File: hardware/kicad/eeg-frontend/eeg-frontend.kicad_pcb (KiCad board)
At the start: 2 copper layers, 60 x 60 mm, 77 parts, among them CN3 1000pF, CN4 1000pF, CN5 1000pF, CN6 1000pF, CN7 1000pF, J1 EEG Connector, J2 Conn_02x06_Top_Bottom, J3 Conn_01x08, J4 Conn_01x02, J5 Conn_01x02, Q1 DMP3099L, U1 ADS1299, U10 TPD4E1B06DCKR, U11 TPD4E1B06DCKR, U2 TPD4E1B06DCKR, U3 LM2664M6/NOPB, U4 MCP1754T-3302E/OT, U5 TPS72325DBV, U6 TLV70025_SOT23-5, U7 TPD4E1B06DCKR, U8 TPD4E1B06DCKR, U9 TPD4E1B06DCKR

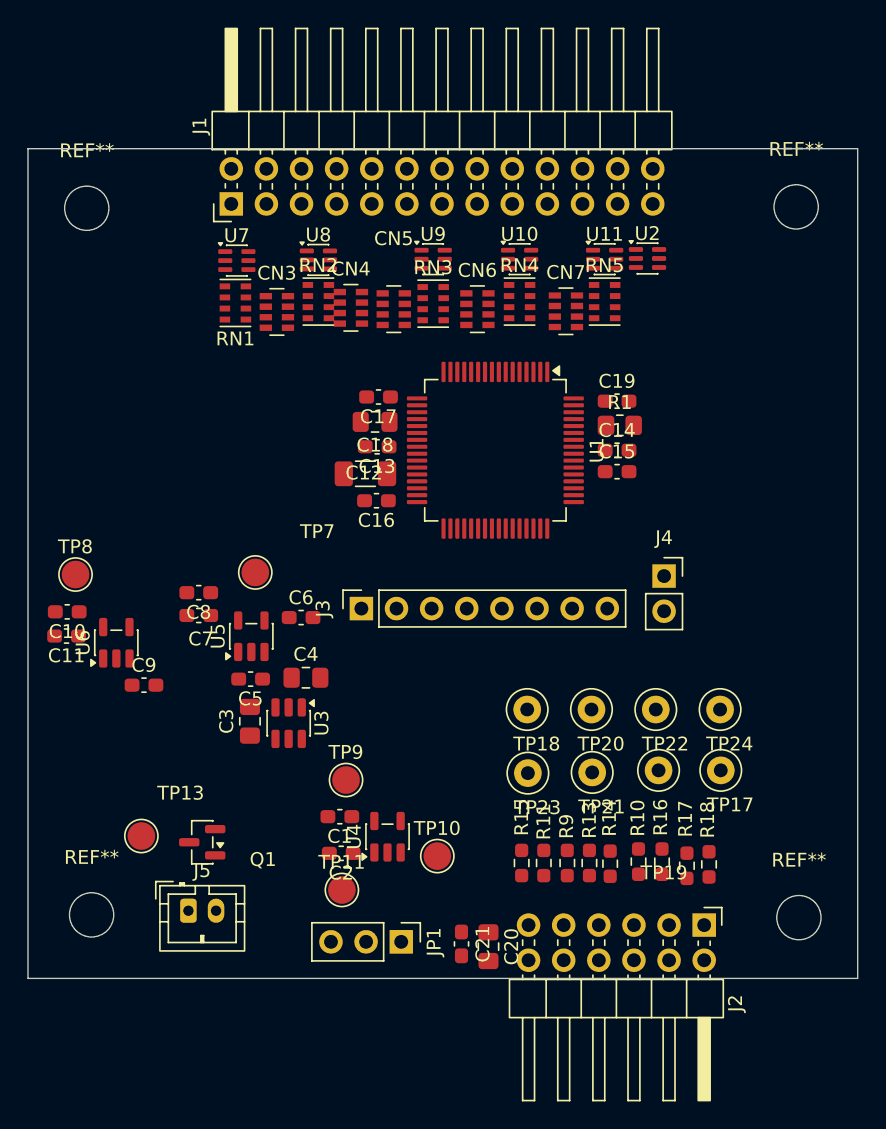
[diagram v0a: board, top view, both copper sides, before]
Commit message: 一旦できたと思ったPCB。 しかしPMODのコネクタの位置が左右で逆で、このまま刺すとGNDの一に通常のデータ信号的なのが来てしまう。
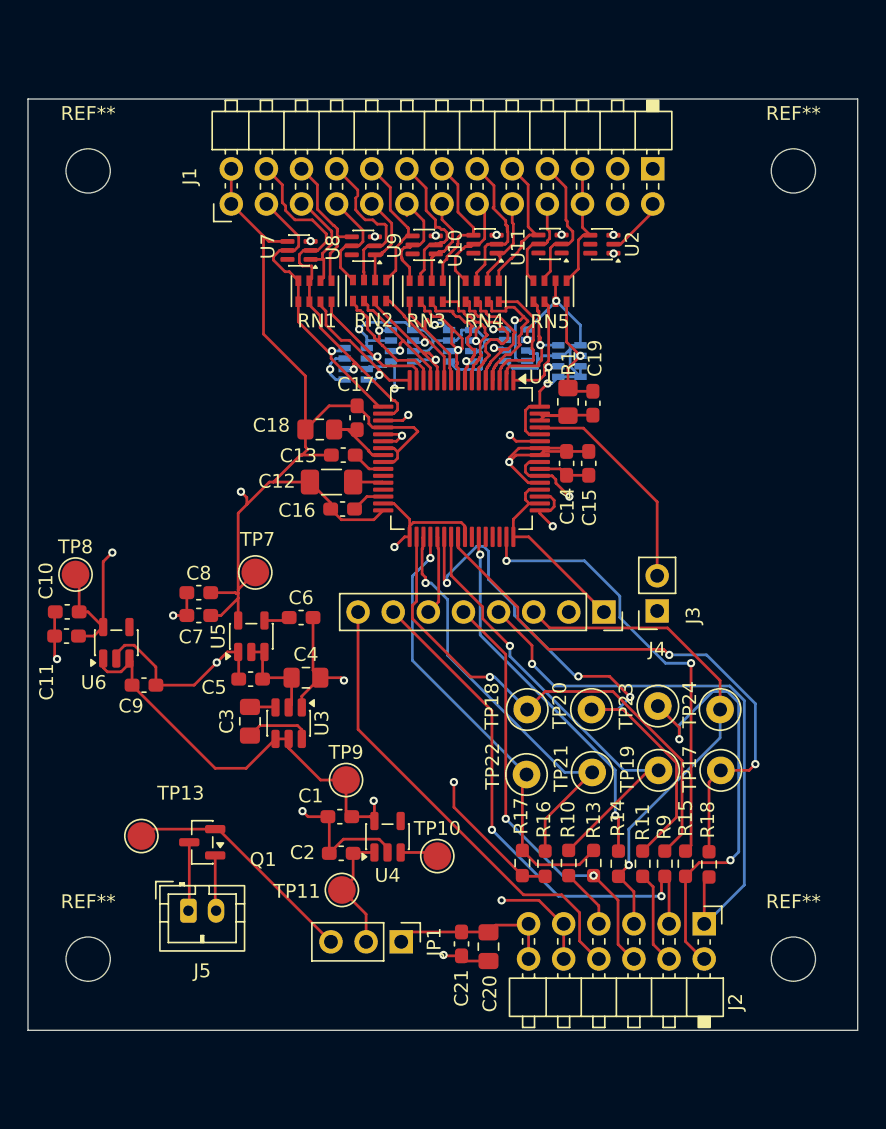
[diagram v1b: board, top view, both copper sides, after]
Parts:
- CN3, CN4, CN5, CN6, CN7: moved to B.Cu
- J1: footprint Connector_PinHeader_2.54mm:PinHeader_2x13_P2.54mm_Horizontal -> myLibrary:PinHeader_2x13_P2.54mm_Horizontal_mirror
- moved J3 17.5 mm to (166.3, 75.9), turned to -90 degrees
- moved R17 11.9 mm to (160.4, 94.0)
- moved R15 11.9 mm to (172.2, 94.1)
- moved TP23 10.6 mm to (170.2, 82.7)
- moved TP22 10.5 mm to (160.7, 87.7)
- moved R16 8.45 mm to (162.1, 94.1)
- moved R11 7.15 mm to (169.1, 94.1)
- moved R9 7.05 mm to (170.7, 94.1)
- moved CN3 6.82 mm to (148.3, 58.0), turned to 180 degrees
- moved RN1 5.81 mm to (145.4, 52.7), turned to 90 degrees
- moved CN5 5.48 mm to (155.9, 56.6), turned to 180 degrees
- moved R10 5.05 mm to (163.8, 94.0)
- moved CN4 4.61 mm to (151.7, 56.6), turned to 180 degrees
- moved U7 4.56 mm to (144.2, 49.8), turned to 180 degrees
- moved R1 4.12 mm to (163.7, 60.7), turned to 90 degrees
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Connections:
- C1 pad 2: GND -> AGND
- C10 pad 2: GND -> AGND
- C11 pad 2: GND -> AGND
- C2 pad 2: GND -> AGND
- C20 pad 2: GND -> AGND
- C21 pad 2: GND -> AGND
- C4 pad 2: GND -> AGND
- C5 pad 2: GND -> AGND
- C6 pad 2: GND -> AGND
- C7 pad 2: GND -> AGND
- C8 pad 2: GND -> AGND
- C9 pad 2: GND -> AGND
- CN3 pad 1: GND -> AGND
- CN3 pad 3: GND -> AGND
- CN3 pad 5: GND -> AGND
- CN3 pad 7: GND -> AGND
- CN4 pad 1: GND -> AGND
- CN4 pad 3: GND -> AGND
- CN4 pad 5: GND -> AGND
- CN4 pad 7: GND -> AGND
- CN5 pad 1: GND -> AGND
- CN5 pad 3: GND -> AGND
- CN5 pad 5: GND -> AGND
- CN5 pad 7: GND -> AGND
- CN6 pad 1: GND -> AGND
- CN6 pad 3: GND -> AGND
- CN6 pad 5: GND -> AGND
- CN6 pad 7: GND -> AGND
- CN7 pad 1: GND -> AGND
- CN7 pad 3: GND -> AGND
- CN7 pad 4: GND -> AGND
- CN7 pad 5: GND -> AGND
- CN7 pad 7: GND -> AGND
- J2 pad 11: PMOD_GND -> AGND
- J2 pad 5: PMOD_GND -> AGND
- J5 pad 2: GND -> AGND
- Q1 pad 1: GND -> AGND
- RN5 pad 3: GND -> AGND
- RN5 pad 4: GND -> AGND
- U1 pad 31: GND -> AGND
- U1 pad 33: GND -> AGND
- U1 pad 41: GND -> AGND
- U1 pad 49: GND -> AGND
- U1 pad 51: GND -> AGND
- U1 pad 60: GND -> AGND
- U1 pad 64: GND -> AGND
- U10 pad 3: GND -> AGND
- U11 pad 3: GND -> AGND
- U2 pad 1: GND -> AGND
- U2 pad 3: GND -> AGND
- U3 pad 1: GND -> AGND
- U4 pad 2: GND -> AGND
- U5 pad 1: GND -> AGND
- U6 pad 2: GND -> AGND
- U7 pad 3: GND -> AGND
- U8 pad 3: GND -> AGND
- U9 pad 3: GND -> AGND
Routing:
- net AGND: track 0.00 -> 130.3 mm, vias 0 -> 21
- net AVSS: track 0.00 -> 86.9 mm, vias 0 -> 2
- net DVDD: track 0.00 -> 56.8 mm, vias 0 -> 2
- net ADS_START: track 0.00 -> 42.5 mm, vias 0 -> 3
- net PMOD_SCLK: track 0.00 -> 42.1 mm, vias 0 -> 1
- net ADS_SCLK: track 0.00 -> 40.7 mm, vias 0 -> 2
- net PMOD_MOSI: track 0.00 -> 38.1 mm, vias 0 -> 2
- net ADS_DIN: track 0.00 -> 37.9 mm, vias 0 -> 1
- net PMOD_MISO: track 0.00 -> 36.6 mm, vias 0 -> 1
- net PMOD_CS2: track 0.00 -> 34.0 mm
- net ADS_CS: track 0.00 -> 33.5 mm, vias 0 -> 1
- net ADS_DRDY: track 0.00 -> 32.8 mm, vias 0 -> 2
- net ADS_RESET: track 0.00 -> 32.8 mm, vias 0 -> 1
- net AVDD: track 0.00 -> 32.2 mm, vias 0 -> 5
- net PMOD_DRDY: track 0.00 -> 31.7 mm, vias 0 -> 2
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- added copper zone on In1.Cu, net AGND
- added copper zone on In2.Cu, net AVDD
- added copper zone on In2.Cu, net AVSS
- added copper zone on In2.Cu, net DVDD
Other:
- board size 60 x 60 mm -> 60 x 67.3 mm
- copper layers 2 -> 4

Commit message: PCBレイアウトが完了
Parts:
- added R12: 0, Resistor_SMD:R_0603_1608Metric_Pad0.98x0.95mm_HandSolder, F.Cu at (146.7, 92.3)
- added TP25: TP_CS2, TestPoint:TestPoint_Loop_D2.50mm_Drill1.0mm, F.Cu at (128.5, 85.8)
- moved TP17 51.6 mm to (128.6, 64.4)
- moved C10 50.1 mm to (177.1, 69.4), turned to 0 degrees
- moved C11 50.1 mm to (177.1, 71.2), turned to 0 degrees
- moved TP13 48.8 mm to (181.6, 92.5)
- moved TP8 48.6 mm to (176.2, 66.2)
- moved U6 46.0 mm to (177.0, 75.7)
- moved TP19 45.3 mm to (128.6, 69.7)
- moved C9 42.7 mm to (175.7, 79.0)
- moved TP24 41.8 mm to (133.0, 80.3)
- moved TP23 41.7 mm to (128.6, 80.3)
- moved R18 39.8 mm to (134.2, 92.3)
- moved Q1 38.5 mm to (175.7, 95.1)
- moved R15 36.3 mm to (136.0, 92.3)
- moved C7 35.7 mm to (172.7, 75.7), turned to 0 degrees
- moved C8 35.7 mm to (172.7, 74.1), turned to 0 degrees
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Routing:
- net ADS_SCLK: track 40.7 -> 74.1 mm
- net ADS_RESET: track 32.8 -> 64.1 mm, vias 1 -> 3
- net ADS_CS: track 33.5 -> 56.6 mm, vias 1 -> 3
- net PMOD_MISO: track 36.6 -> 58.7 mm
- net ADS_CS2: track 0.00 -> 20.5 mm
- net ADS_DRDY: track 32.8 -> 48.9 mm
- net BIAS_INV: track 16.1 -> 31.9 mm, vias 0 -> 1
- net ADS_DIN: track 37.9 -> 53.7 mm, vias 1 -> 2
- net ADS_PWDN: track 30.7 -> 44.2 mm, vias 1 -> 2
- net AGND: track 130.3 -> 141.5 mm, vias 21 -> 22
- net ADS_START: track 42.5 -> 53.1 mm
- net ADS_DOUT: track 26.9 -> 36.4 mm
- net PMOD_CS2: track 34.0 -> 42.9 mm
- net VIN_SYS: track 9.02 -> 17.5 mm
- net PMOD_MOSI: track 38.1 -> 30.6 mm
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
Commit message: PCBエディタ上に各部品のManufacturerとPart Number、とついでにDNP(実装するかどうか)を掲載した。
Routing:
- net ADS_SCLK: track 74.1 -> 101.2 mm

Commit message: DigikeyでSAMSUNGのキャパシタが売り切れだったので村田のキャパシタに変更
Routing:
- net ADS_SCLK: track 101.2 -> 74.1 mm
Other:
- board text added: "Closed-Loop Neural Interface Project"
- board text added: "EEG Interface Board Rev.1 Designed by Takashi Ikejima"
